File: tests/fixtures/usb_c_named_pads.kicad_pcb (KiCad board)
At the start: 2 copper layers, 35 x 20 mm, 2 parts, among them J1 USB_C_Receptacle_USB2.0

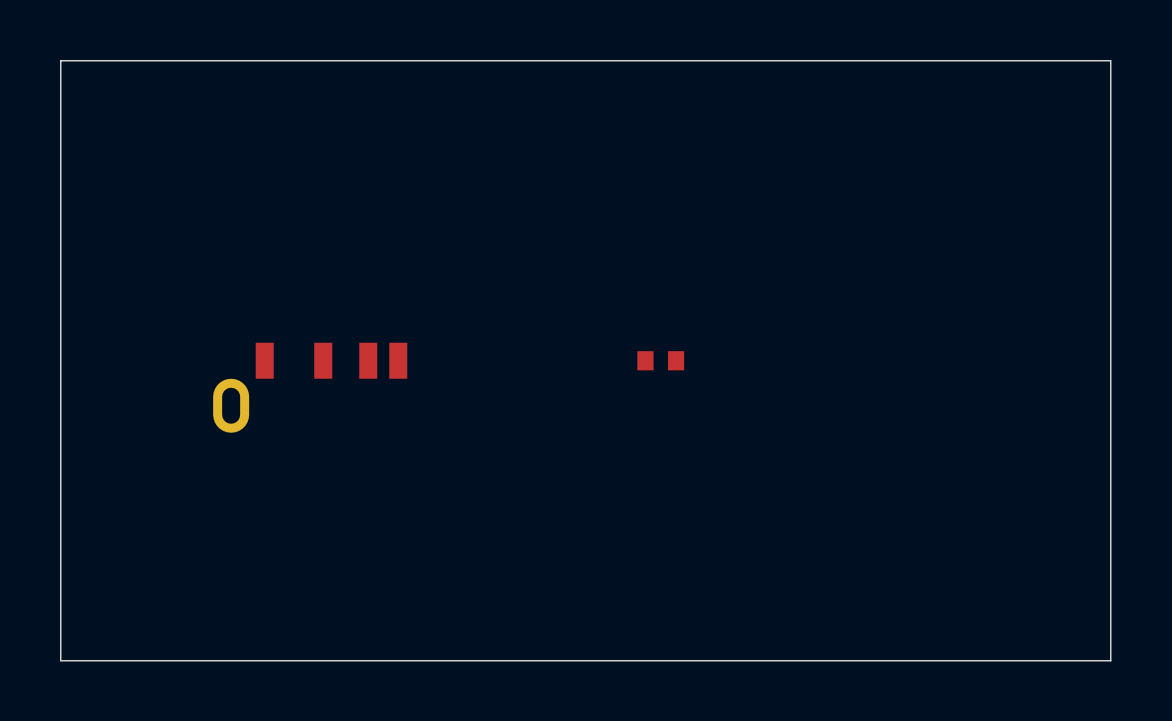
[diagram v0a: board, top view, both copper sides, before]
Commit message: feat(parser): let a zone be named the way its net is named
A pour is usually named after the net it fills, and the net that most
often needs quoting is the power rail. `zone_net` had already learned
about quotes; the zone *name* had not - `zone_definition` took an
identifier - so a board with a `GND` plane and a `VBUS+` plane came back
with one of them and `// one zone named "VBUS+" is not written: the
grammar takes an identifier for a zone name and has no quoted form`
where the other should have been.

One rule in three places: `net_name`, the choice of an identifier or a
quoted string, is what the zone name takes in the grammar (regenerated
with `npx tree-sitter generate`), in the hand-written reader, and in
`dsl.rs`, which no longer needs a branch for describing what it could
not write. README said a pour has no syntax in the language yet; it has
had one, and what it lacked was a name it could keep.

Proof:

    cypcb from-kicad tests/fixtures/usb_c_named_pads.kicad_pcb
    before -> zone GND { ... } and a comment where the other plane was
    after  -> zone GND { ... } and zone "VBUS+" { ... }

    cargo test -p cypcb-cli --test a_pour_named_after_its_net_comes_back
    -> 3 passed
    cargo test -p cypcb-parser --features tree-sitter-parser --test differential
    -> 3 passed; --test error_parity -> 5 passed

Mutations, each alone against a clean tree and restored from the saved
file:

    the reader's zone name back to `identifier` -> 3 failed, the import
      stops because what it wrote will not read back
    the writer emitting the zone name bare -> 3 failed, the same way

    ./scripts/quality-gate.sh -> === All stages passed ===
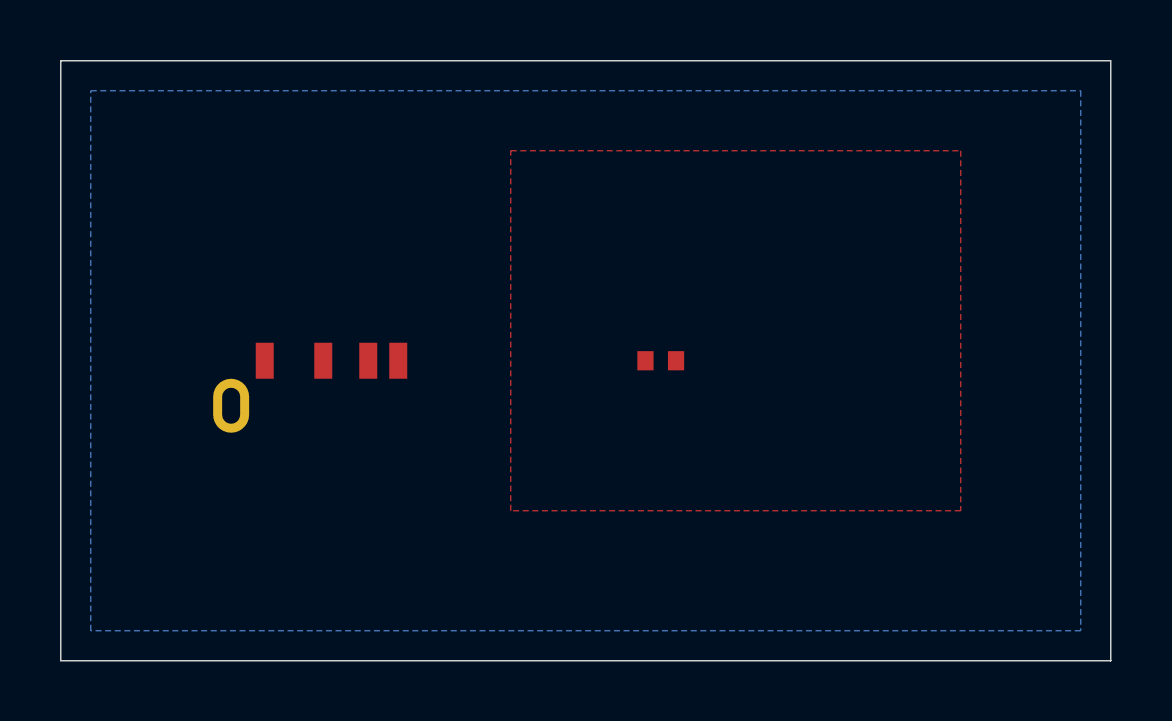
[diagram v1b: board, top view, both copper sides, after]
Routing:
- added copper zone on B.Cu, net GND
- added copper zone on F.Cu, net VBUS+
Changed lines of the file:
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@@
   (gr_line (start 45 25) (end 10 25) (layer "Edge.Cuts") (width 0.05))
   (gr_line (start 10 25) (end 10 5) (layer "Edge.Cuts") (width 0.05))
+  (zone
+    (net 2)
+    (net_name "GND")
+    (layer "B.Cu")
+    (hatch edge 0.5)
+    (connect_pads (clearance 0.5))
+    (min_thickness 0.25)
+    (fill yes (thermal_gap 0.5) (thermal_bridge_width 0.5))
+    (polygon
+      (pts
+        (xy 11 6) (xy 44 6) (xy 44 24) (xy 11 24)
+      )
+    )
+  )
+  (zone
+    (net 1)
+    (net_name "VBUS+")
+    (layer "F.Cu")
+    (hatch edge 0.5)
+    (connect_pads (clearance 0.5))
+    (min_thickness 0.25)
+    (fill yes (thermal_gap 0.5) (thermal_bridge_width 0.5))
+    (polygon
+      (pts
+        (xy 25 8) (xy 40 8) (xy 40 20) (xy 25 20)
+      )
+    )
+  )
 )

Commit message: fix(cli): say which pours from-kicad could not carry
The importer refuses a pour it cannot state - an L cut around a
connector is not a rectangle, and a bounding box would put copper where
the shape was drawn to avoid it - and it says why in
`metadata.zone_refusals`. The browser engine has printed those reasons
since they existed. `from-kicad` did not: a board came through the
command line one ground plane short, reporting `2 component(s), 3
net(s), 2 footprint definition(s)` as if nothing had happened.

Both refusal lists, zones and stackup, are reported on stderr now. The
USB fixture gained an L-shaped ground plane cut around the receptacle,
so one file holds two pours that arrive and one that cannot.

Proof:

    cypcb from-kicad tests/fixtures/usb_c_named_pads.kicad_pcb
    before -> the summary line only
    after  -> Warning: the zone on net GND is a 6-point outline; this
              importer carries rectangular pours only, and a bounding box
              would put copper where the shape was drawn to avoid it

    cargo test -p cypcb-cli --test a_pour_the_importer_cannot_carry_is_named
    -> 2 passed

Mutations, each alone against a clean tree and restored from the saved
file:

    the reporting loop removed -> 1 failed
    axis_aligned_rectangle approximating any outline by its bounding box
    -> 2 failed: the missing warning, and the design has three pours
       where it should have two

The first attempt at that second mutation dropped only the four-point
guard and passed - the corner check refuses a six-point outline on its
own, and the test said so by not moving.

    ./scripts/quality-gate.sh -> === All stages passed ===
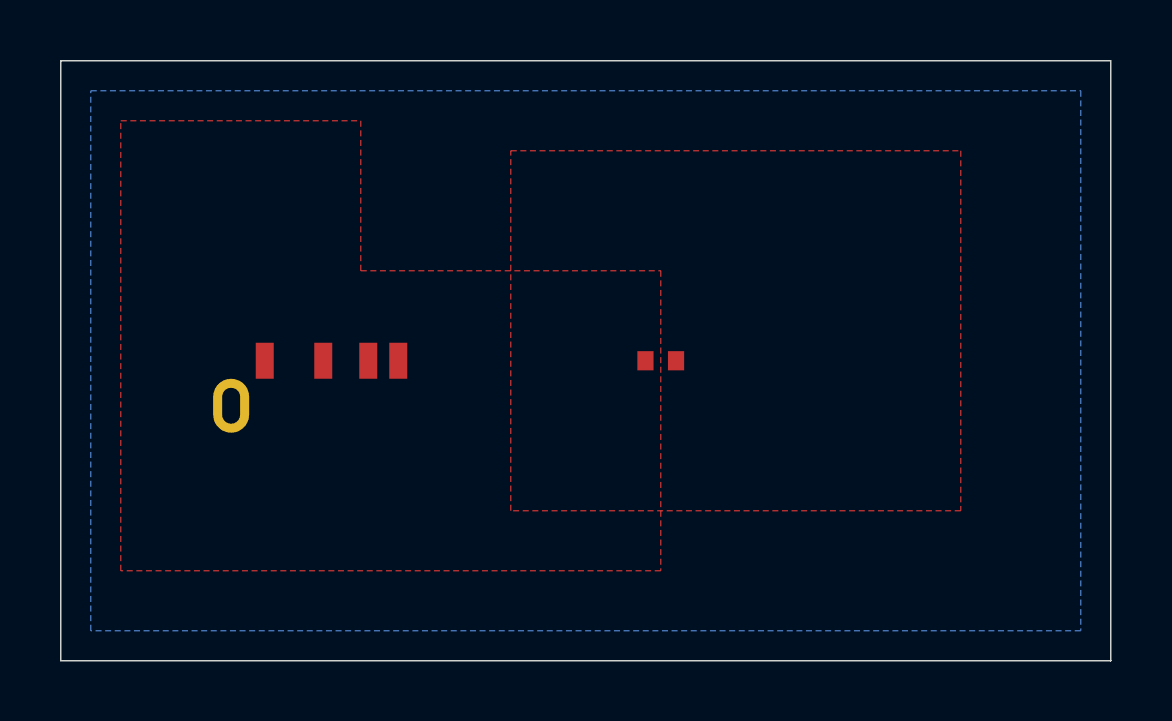
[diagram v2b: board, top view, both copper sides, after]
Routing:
- added copper zone on F.Cu, net GND
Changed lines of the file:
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@@
+    )
+  )
+  (zone
+    (net 2)
+    (net_name "GND")
+    (layer "F.Cu")
+    (hatch edge 0.5)
+    (connect_pads (clearance 0.5))
+    (min_thickness 0.25)
+    (fill yes (thermal_gap 0.5) (thermal_bridge_width 0.5))
+    (polygon
+      (pts
+        (xy 12 7) (xy 20 7) (xy 20 12) (xy 30 12) (xy 30 22) (xy 12 22)
+      )
     )
   )
